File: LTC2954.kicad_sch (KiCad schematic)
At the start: 21 parts, among them SW2 SW_Push, U1 LTC2954CTS8-2_TRPBF

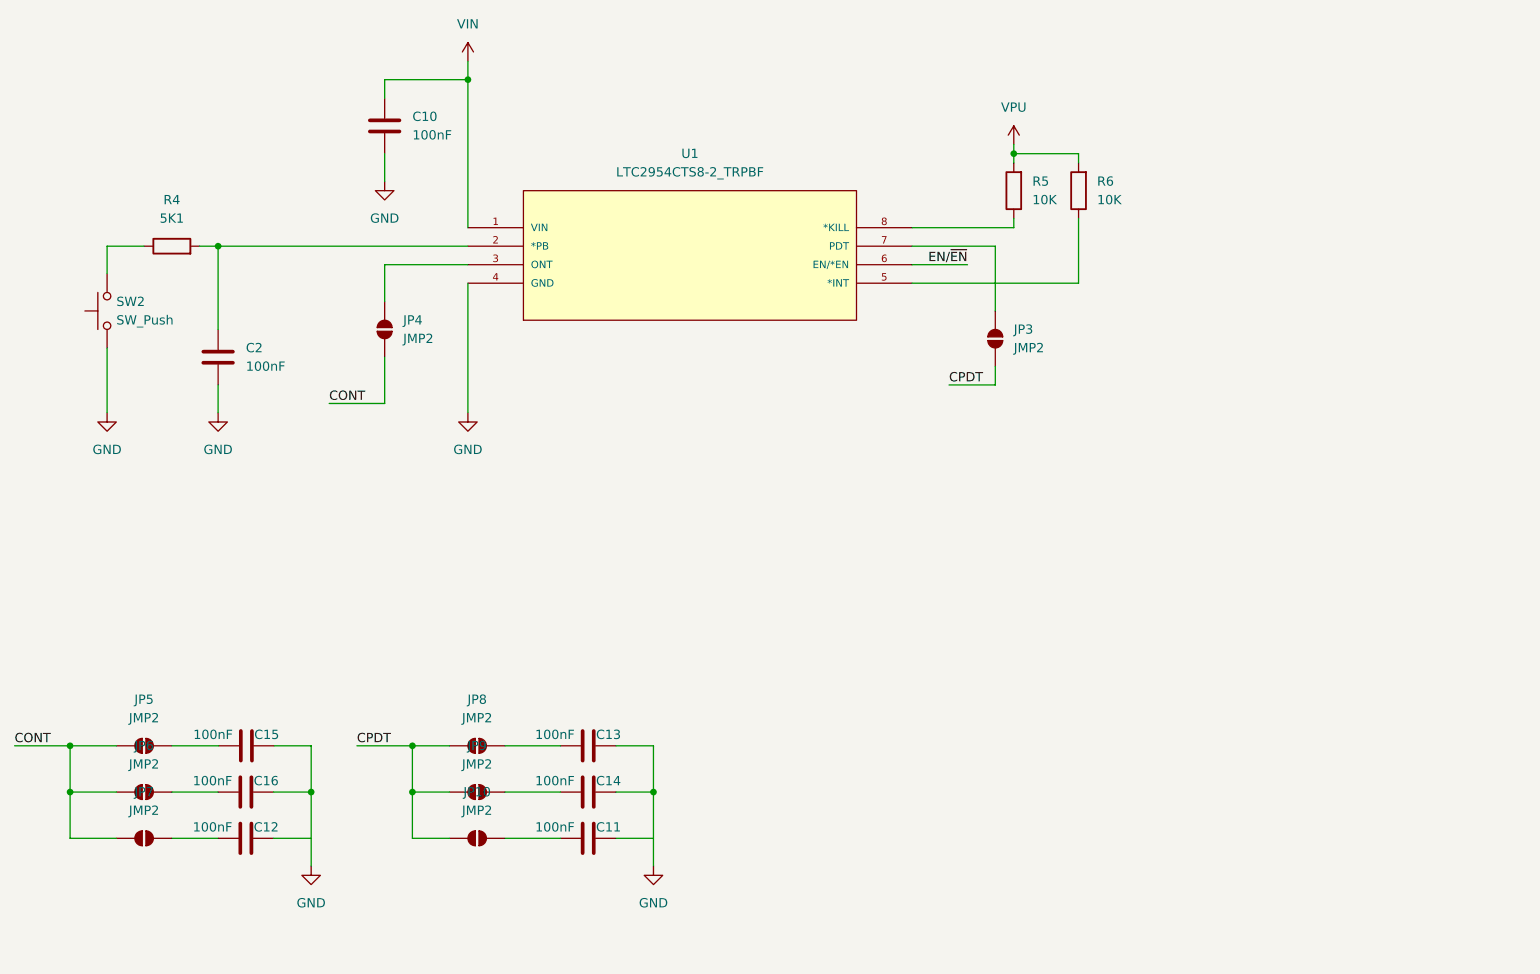
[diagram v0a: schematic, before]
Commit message: Added B.O.M, TODO: do PCB track layout
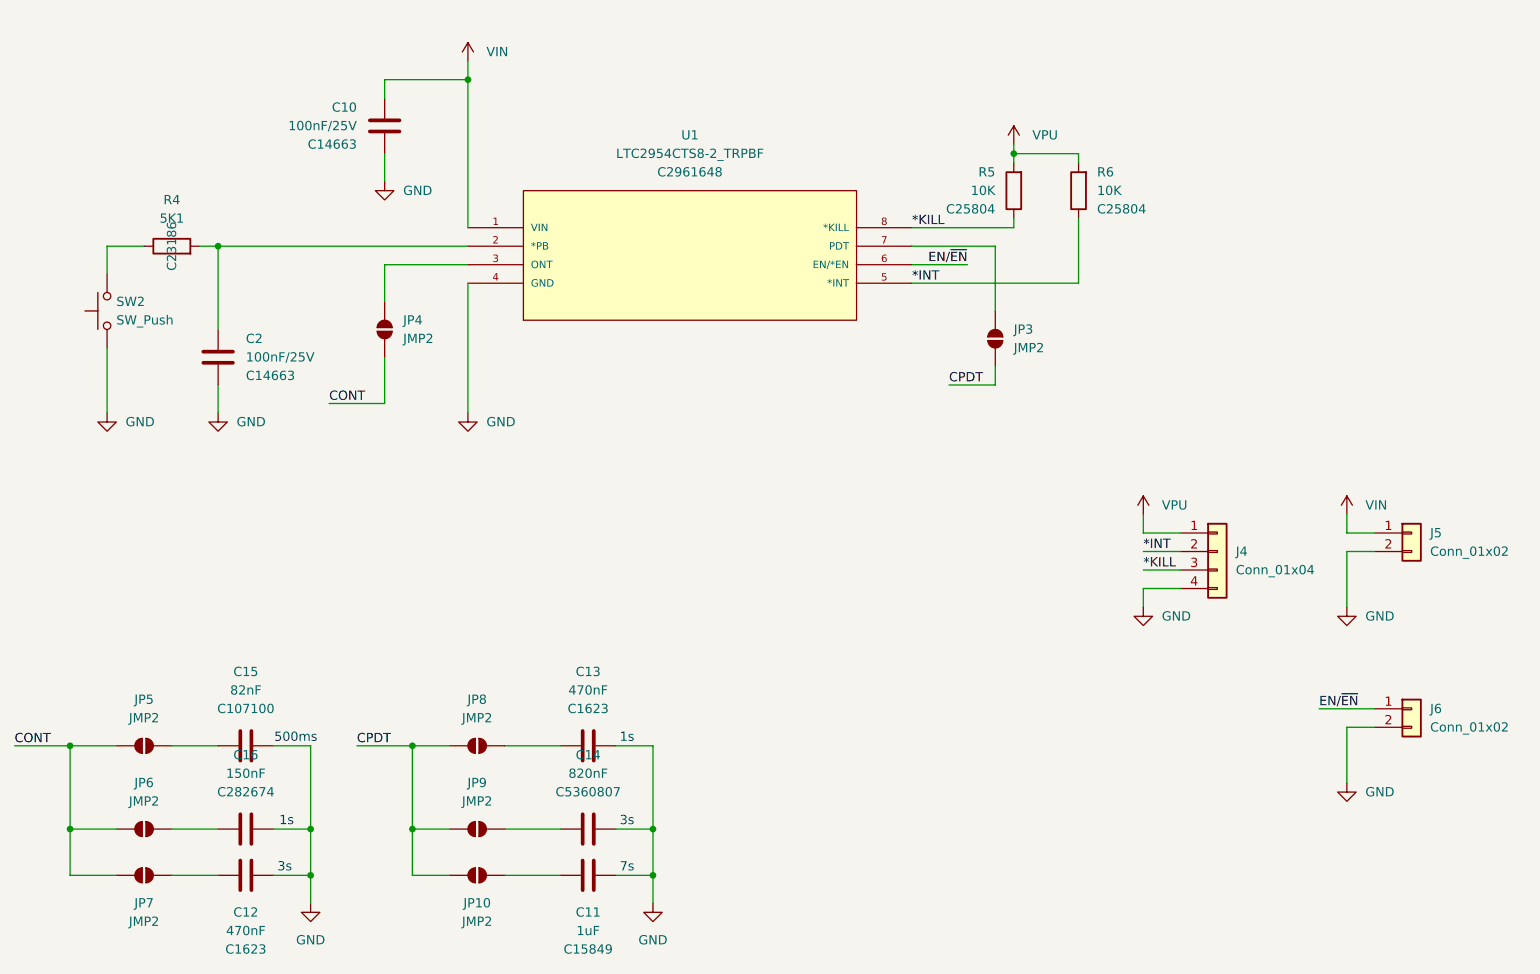
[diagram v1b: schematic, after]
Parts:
- added J4: Conn_01x04, Connector_PinHeader_2.54mm:PinHeader_1x04_P2.54mm_Vertical, symbol Connector_Generic:Conn_01x04
- added J5, J6: Conn_01x02, Connector_PinHeader_2.54mm:PinHeader_1x02_P2.54mm_Vertical, symbol Connector_Generic:Conn_01x02
- C10, C2: value 100nF -> 100nF/25V; JLCPCB Part # (none) -> C14663
- C11: value 100nF -> 1uF; JLCPCB Part # (none) -> C15849
- C12, C13: value 100nF -> 470nF; JLCPCB Part # (none) -> C1623
- C14: value 100nF -> 820nF; JLCPCB Part # (none) -> C5360807
- C15: value 100nF -> 82nF; JLCPCB Part # (none) -> C107100
- C16: value 100nF -> 150nF; JLCPCB Part # (none) -> C282674
- R4: JLCPCB Part # (none) -> C23186
- R5, R6: JLCPCB Part # (none) -> C25804
- U1: JLCPCB Part # (none) -> C2961648
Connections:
- net EN/~{EN}: now also J6.1 (Pin_1)
- net GND: now also C11.2, C12.2, J4.4 (Pin_4), J5.2 (Pin_2), J6.2 (Pin_2)
- net VIN: now also J5.1 (Pin_1)
- net VPU: now also J4.1 (Pin_1)
- net *KILL: now reaches R5.1, U1.8 (*KILL)
- net *KILL: now also J4.3 (Pin_3)
- net *INT: now reaches R6.1, U1.5 (*INT)
- net *INT: now also J4.2 (Pin_2)
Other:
- note added: "1s"
- note added: "3s"
- note added: "500ms"
- note added: "7s"
- moved on the sheet: C11, C12, C14, C16, JP10, JP6, JP7, JP9

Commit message: Finished, 1st PCB order to JLCPCB
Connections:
- net VIN renamed VIN_2954
- net VPU renamed VPU_2954
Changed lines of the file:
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@@
 			)
 		)
-		(property "Value" "VPU"
-			(at 198.12 54.6099 0)
-			(effects
-				(font
-					(size 1.27 1.27)
-				)
-				(justify left)
+		(property "Value" "VPU_2954"
+			(at 195.58 50.8 0)
+			(effects
+				(font
+					(size 1.27 1.27)
+				)
 			)
 		)
@@
 			)
 		)
-		(property "Value" "VIN"
-			(at 123.19 43.1799 0)
-			(effects
-				(font
-					(size 1.27 1.27)
-				)
-				(justify left)
+		(property "Value" "VIN_2954"
+			(at 120.65 39.37 0)
+			(effects
+				(font
+					(size 1.27 1.27)
+				)
 			)
 		)
@@
 			)
 		)
-		(property "Value" "VPU"
-			(at 215.9 105.4099 0)
-			(effects
-				(font
-					(size 1.27 1.27)
-				)
-				(justify left)
+		(property "Value" "VPU_2954"
+			(at 213.36 101.6 0)
+			(effects
+				(font
+					(size 1.27 1.27)
+				)
 			)
 		)
@@
 			)
 		)
-		(property "Value" "VIN"
-			(at 243.84 105.4099 0)
-			(effects
-				(font
-					(size 1.27 1.27)
-				)
-				(justify left)
-			)
-		)
+		(property "Value" "VIN_2954"
+			(at 241.3 101.6 0)
+			(effects
+				(font
+					(size 1.27 1.27)
+				)
+			)
+		)
